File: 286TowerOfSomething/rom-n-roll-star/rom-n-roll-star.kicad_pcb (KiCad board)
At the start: 2 copper layers, 15 parts, among them J1 Bus_ISA_8bit, SW1 SW_DIP_x08, U1 SST39SF010, U2 74ALS688

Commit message: Finished routing?
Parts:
- moved R1 55.2 mm to (139.7, 78.7), turned to 0 degrees
- moved R2 53.4 mm to (139.7, 76.2), turned to 180 degrees
- moved R3 52.7 mm to (139.7, 61.0), turned to 180 degrees
- moved C3 52.1 mm to (150.5, 80.0)
- moved R8 52.1 mm to (139.7, 73.7), turned to 180 degrees
- moved R4 51.6 mm to (139.7, 63.5), turned to 180 degrees
- moved R7 51.2 mm to (139.7, 71.1), turned to 180 degrees
- moved R5 50.9 mm to (139.7, 66.0), turned to 180 degrees
- moved R6 50.8 mm to (139.7, 68.6), turned to 180 degrees
- moved C2 47.4 mm to (123.2, 85.1), turned to -90 degrees
- moved SW1 45.5 mm to (135.9, 61.0), turned to 0 degrees
- moved U2 42.4 mm to (130.8, 81.3), turned to 180 degrees
- moved C1 27.1 mm to (114.3, 81.3), turned to -90 degrees
- moved U1 23.8 mm to (114.3, 62.2), turned to -90 degrees
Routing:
- net +5V: track 0.00 -> 83.4 mm, vias 0 -> 4
- net /D2: track 19.7 -> 97.2 mm, vias 1 -> 3
- net /D1: track 19.7 -> 93.1 mm, vias 1 -> 3
- net /D0: track 20.7 -> 87.0 mm, vias 0 -> 3
- net /D4: track 19.7 -> 82.6 mm, vias 1 -> 2
- net /D5: track 19.7 -> 82.6 mm, vias 1 -> 2
- net /D3: track 19.7 -> 81.8 mm, vias 1 -> 2
- net /D6: track 20.7 -> 82.6 mm, vias 0 -> 2
- net /D7: track 24.8 -> 82.6 mm, vias 1 -> 2
- net /~{MEMWR}: track 0.00 -> 54.0 mm, vias 0 -> 2
- net /~{MEMRD}: track 0.00 -> 51.0 mm, vias 0 -> 1
- net /FLASH_A15: track 2.86 -> 45.3 mm, vias 0 -> 3
- net /~{ROMWE}: track 2.86 -> 43.5 mm, vias 0 -> 3
- net /A3: track 0.00 -> 38.5 mm
- net /A1: track 0.00 -> 38.5 mm
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- added copper zone on B.Cu, net GND
- added copper zone on F.Cu, net GND
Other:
- board outline added: 81.3 x 44.4 mm

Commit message: Adding silkscreen to rom-n-roll-star
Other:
- board text added: "32KiB mappings"
- board text added: "64KiB mappings"
- board text added: "Address Select"
- board text added: "Base Sw3 Sw4 Sw5 Sw6 Sw7 Sw8 8000h* On On On On Off On 8800h* Off On On On Off On 9000h* On Off On On Off On 9800h* Off Off On On Off On A000h On On Off On Off On A800h Off On Off On Off On B000h On Off Off On Off On B800h Off Off Off On Off On"
- board text added: "Base Sw3 Sw4 Sw5 Sw6 Sw7 Sw8 8000h* On On On On On Off 9000h* On Off On On On Off A000h On On Off On On Off B000h On Off Off On On Off C000h On On On Off On Off D000h On Off On Off On Off E000h On On Off Off On Off F000h On Off Off Off On Off"
- board text added: "Base Sw3 Sw4 Sw5 Sw6 Sw7 Sw8 C000h On On On Off Off On C800h Off On On Off Off On D000h On Off On Off Off On D800h Off Off On Off Off On E000h On On Off Off Off On E800h Off On Off Off Off On F000h On Off Off Off Off On F800h Off Off Off Off Off On"
- board text added: "ROM Enable"
- board text added: "ROM Write Enable"
- board text added: "ROM-n-Roll Star 2024-09-25 by rglenn"

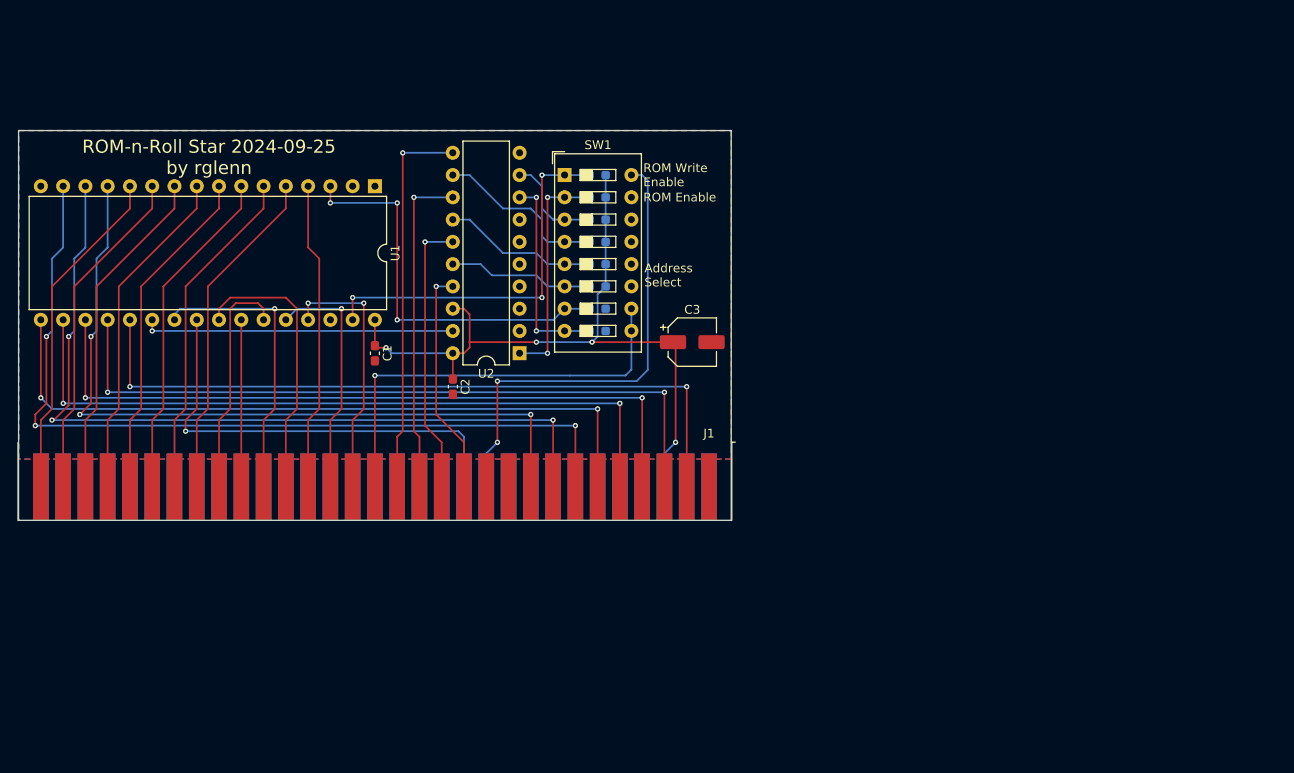
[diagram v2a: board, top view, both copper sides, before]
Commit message: Adding ISA bracked to rom-n-roll-star
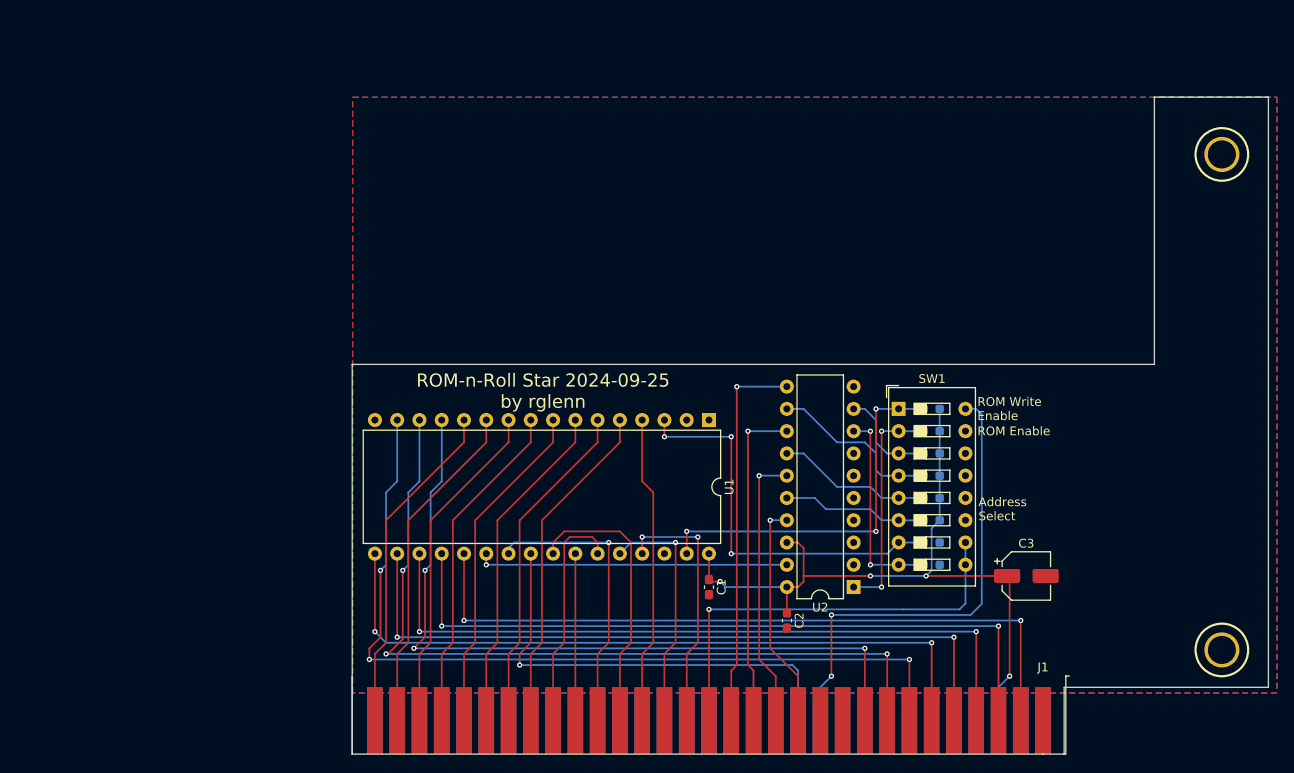
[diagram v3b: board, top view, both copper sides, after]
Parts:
- added BRACKET1: ~, pc-parts:PC_BRACKET_ISA_KEYSTONE_9202_Rev1, F.Cu at (190.5, 127.0)
- moved R1 46.5 mm to (177.8, 105.4)
- moved R2 46.5 mm to (177.8, 102.9)
- moved R4 46.5 mm to (177.8, 90.2)
- moved R6 46.5 mm to (177.8, 95.2)
- moved R7 46.5 mm to (177.8, 97.8)
- moved R8 46.5 mm to (177.8, 100.3)
- moved C1 46.5 mm to (152.4, 108.0)
- moved R3 46.5 mm to (177.8, 87.6)
- moved R5 46.5 mm to (177.8, 92.7)
- moved U1 46.5 mm to (152.4, 88.9)
- moved C2 46.5 mm to (161.3, 111.8)
- moved C3 46.5 mm to (188.6, 106.7)
- moved J1 46.5 mm to (190.5, 123.2)
- moved SW1 46.5 mm to (174.0, 87.6)
- moved U2 46.5 mm to (168.9, 107.9)
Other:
- board size 81.3 x 44.4 mm -> 104.5 x 74.9 mm
